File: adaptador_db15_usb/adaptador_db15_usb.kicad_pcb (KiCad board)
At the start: 2 copper layers, 57.7 x 30.8 mm, 3 parts, among them J1 Conn_01x34, J2 A-USB3_A-LP-SMT1, J3 A-USB3_A-LP-SMT1

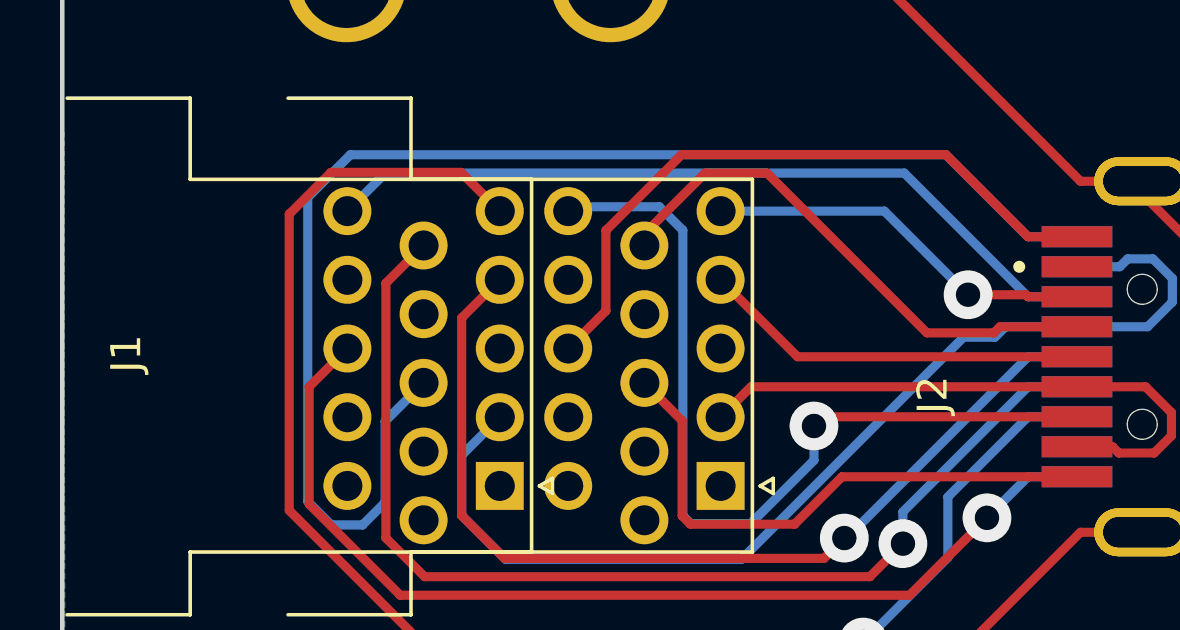
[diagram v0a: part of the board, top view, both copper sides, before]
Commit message: Arrumado Silk screen
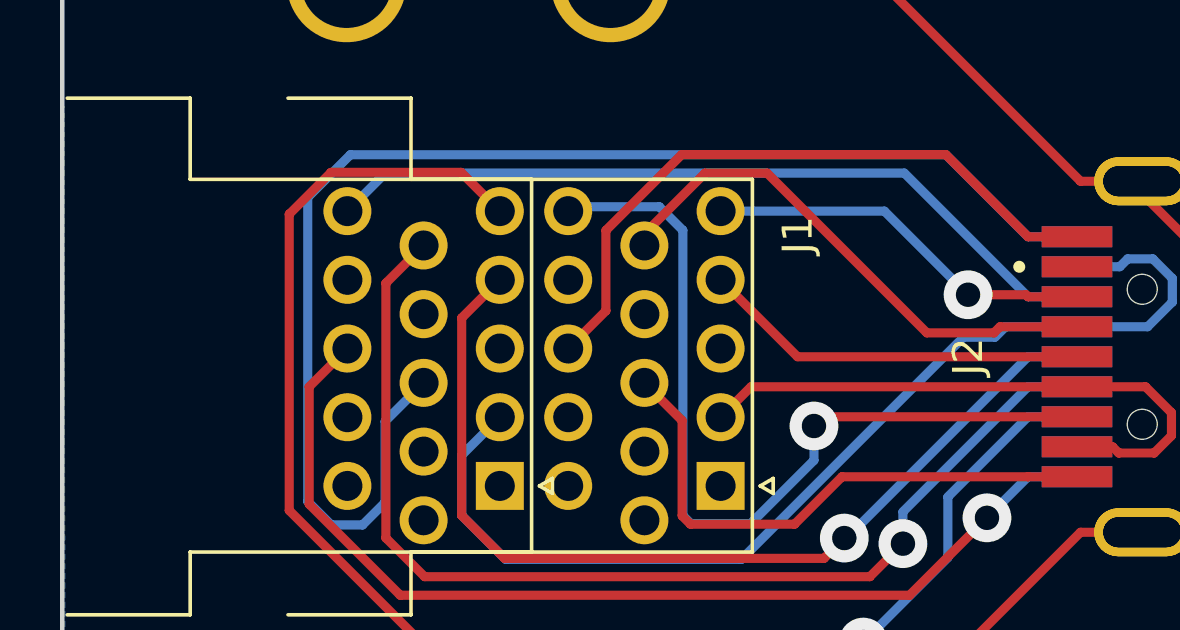
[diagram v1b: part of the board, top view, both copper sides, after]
